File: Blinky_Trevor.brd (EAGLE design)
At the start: 101.6 x 101.3 mm, 15 parts, among them IC1 OP-DUALRM

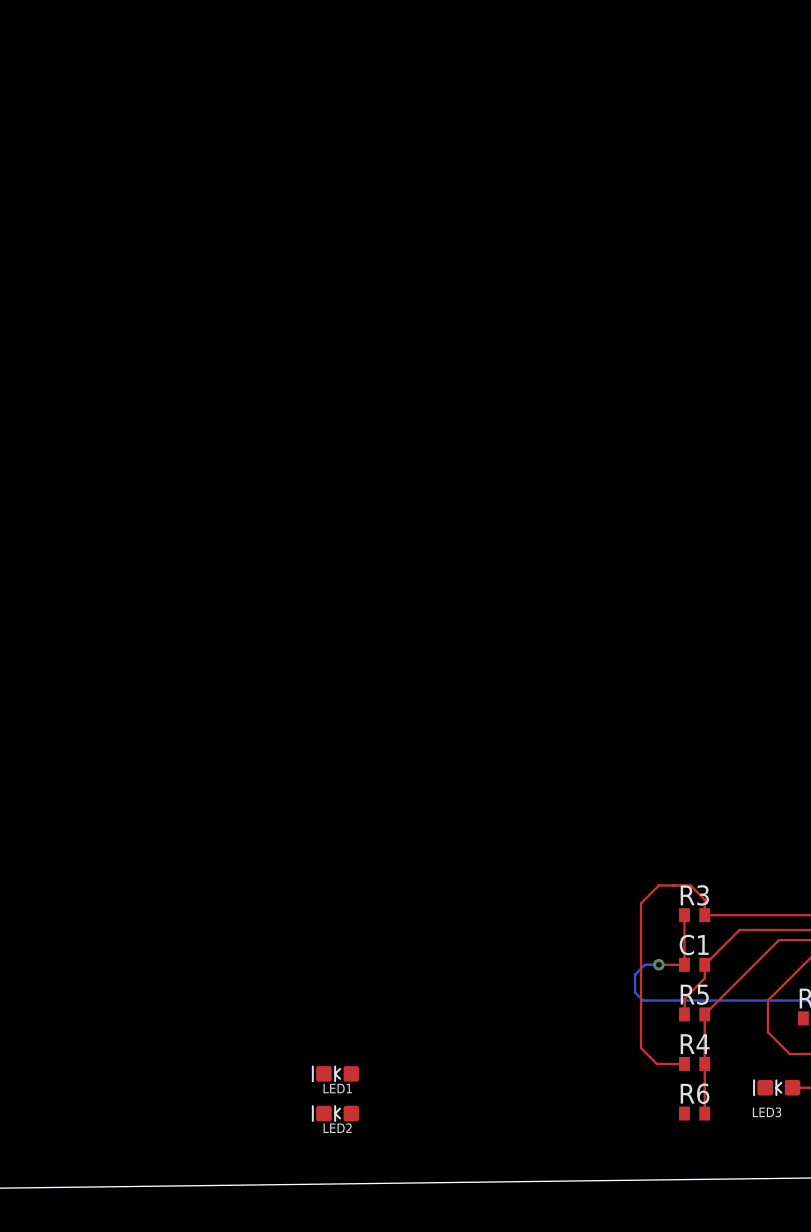
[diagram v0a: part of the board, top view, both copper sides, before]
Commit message: Added LED Pattern
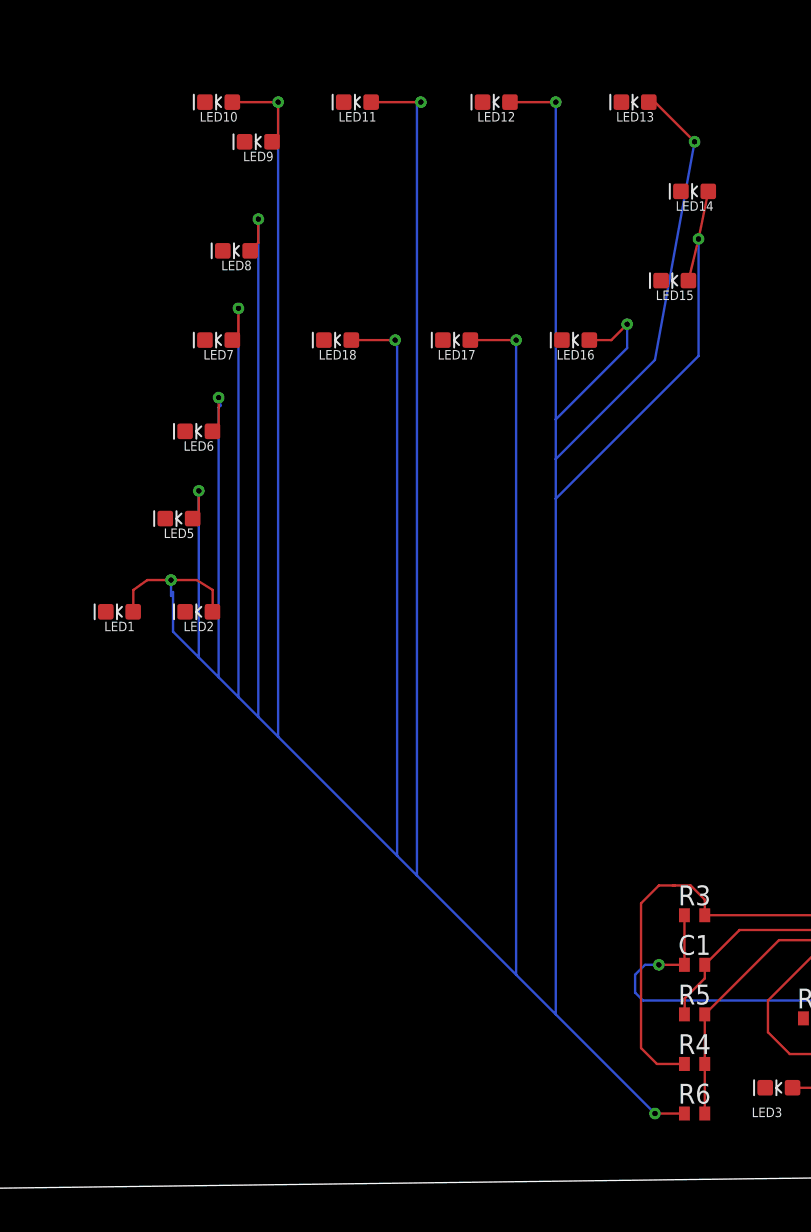
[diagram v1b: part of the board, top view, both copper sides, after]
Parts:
- added LED10, LED11, LED12, LED13, LED14, LED15, LED16, LED17, LED18, LED5, LED6, LED7, LED8, LED9: (no value), CalvEngIO-LED:LED-0603
- moved LED2 33.3 mm to (36.8, 37.2)
- moved LED1 32.7 mm to (31.8, 37.2)
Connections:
- net GND: now also LED10.C, LED11.C, LED12.C, LED13.C, LED14.C, LED15.C, LED16.C, LED17.C, LED18.C, LED5.C, LED6.C, LED7.C, LED8.C, LED9.C
- net N$6: now also LED10.A, LED11.A, LED12.A, LED13.A, LED14.A, LED15.A, LED16.A, LED17.A, LED18.A, LED5.A, LED6.A, LED7.A, LED8.A, LED9.A
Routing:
- net N$6: track 0.00 -> 456.6 mm, vias 0 -> 14
